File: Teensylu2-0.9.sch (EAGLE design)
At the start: 113 parts, among them J1 12VPWR, J10 HOTEND-2, J11 E1-THRM, J12 B-THRM, J13 E2-THRM, J2 MICROSD, J3 USB-MICRO-PTH, J4 FAN, J5 4P-TERM-BLOCK284391-4, J6 39-29-3066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

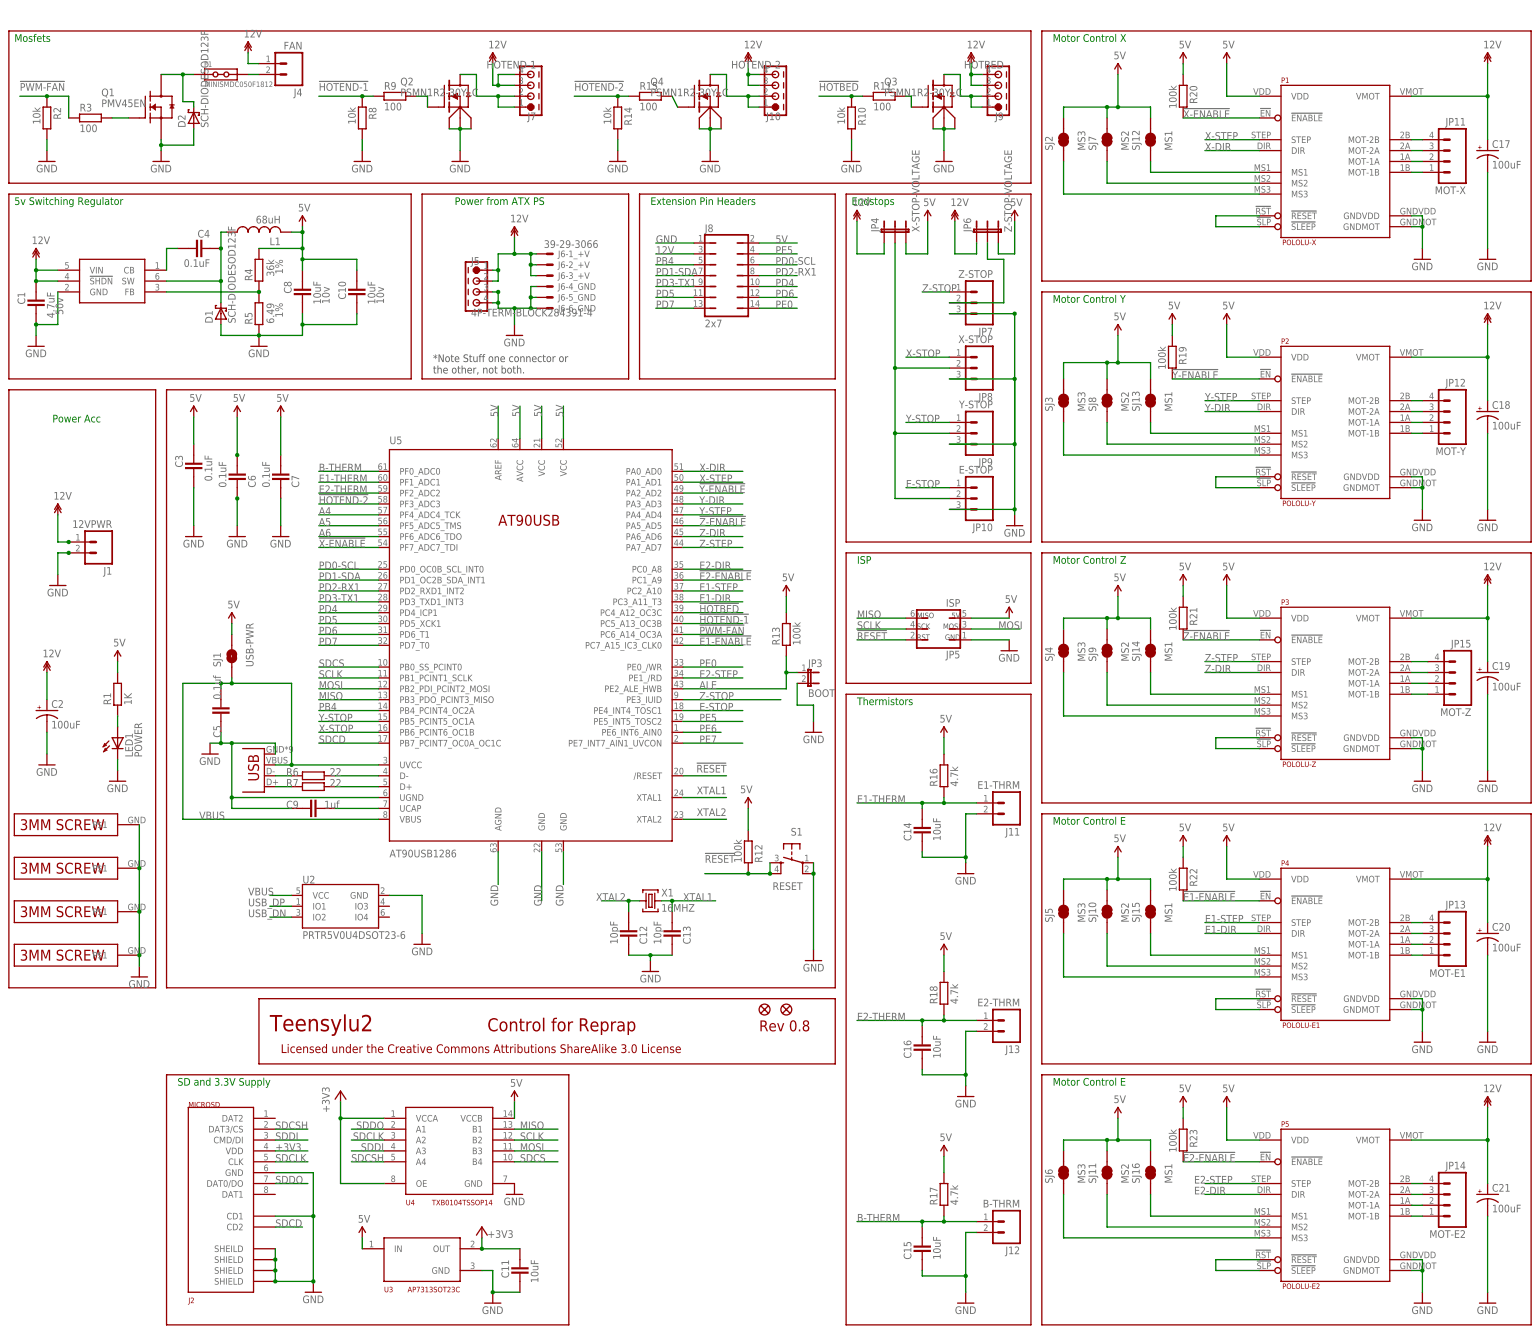
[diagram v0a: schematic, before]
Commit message: Production release
Pin mapping is added. Had to move a lot of pins around due to limitation
of the Teensyduino library.
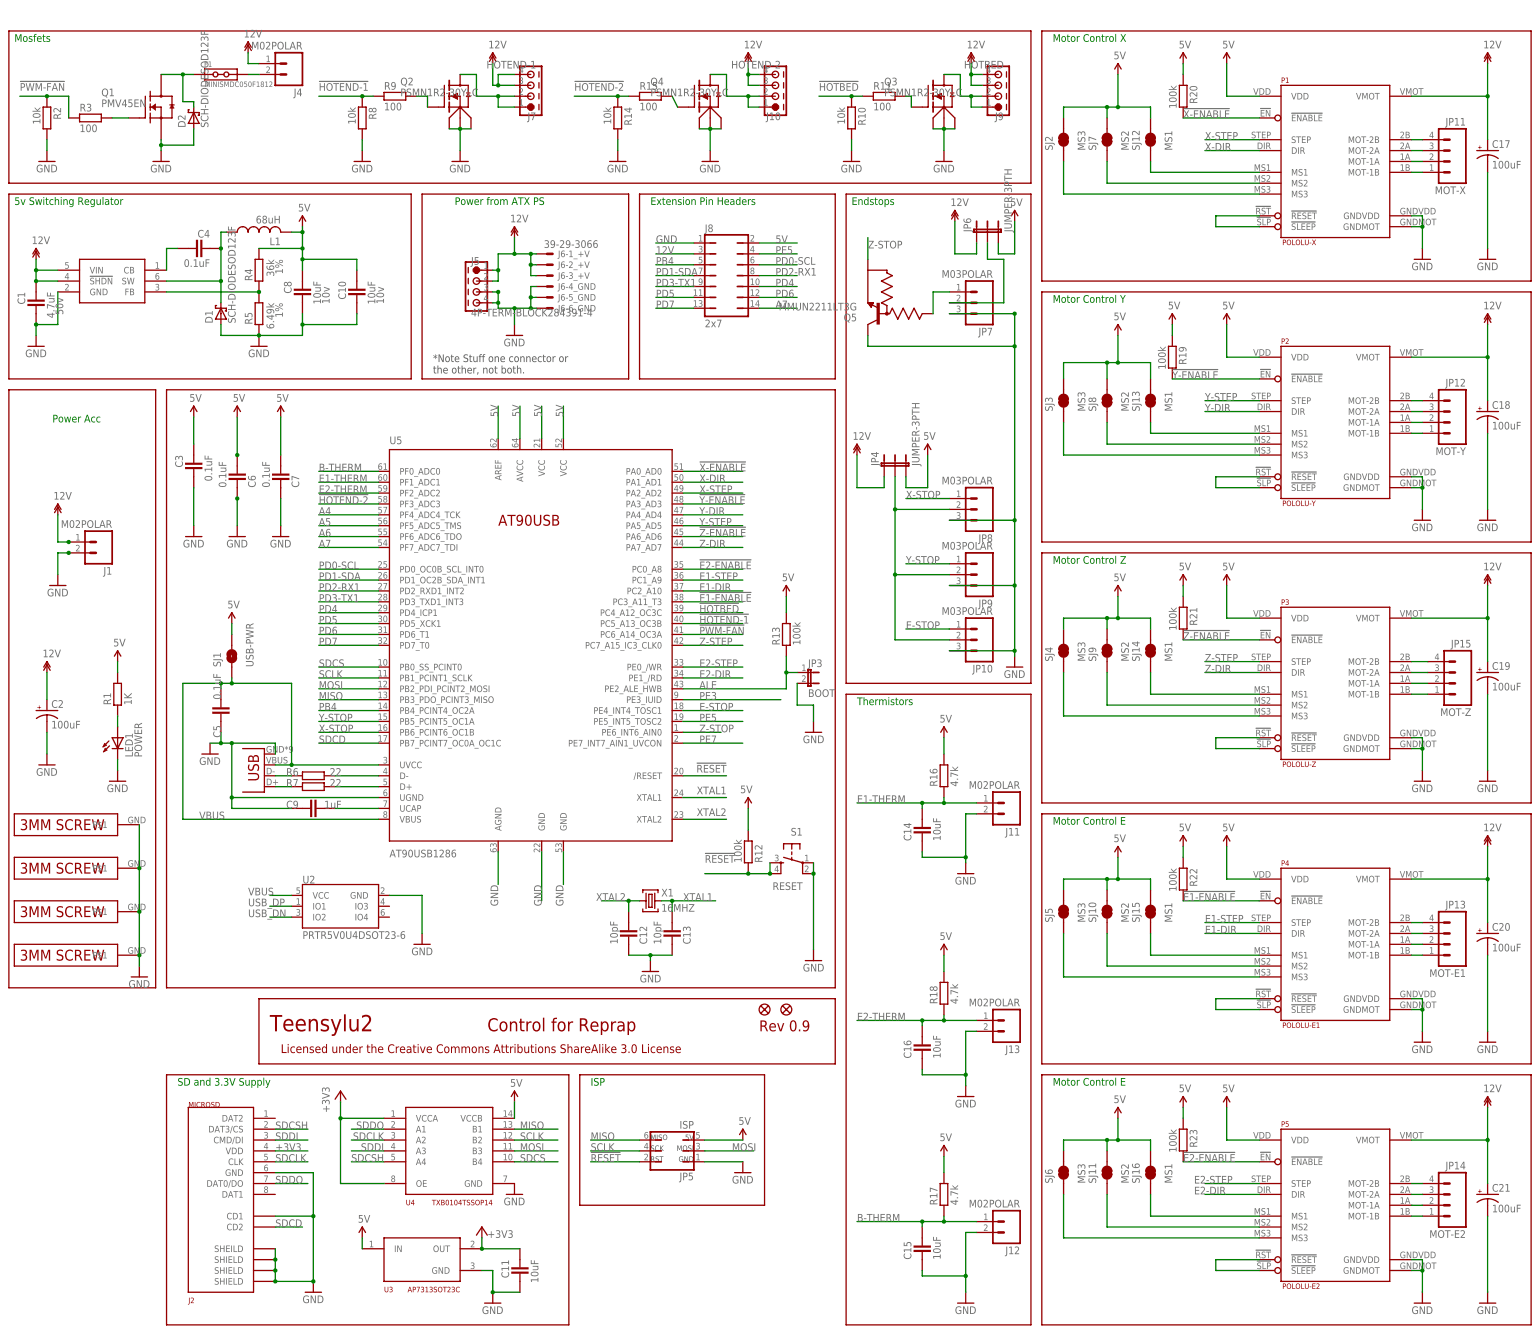
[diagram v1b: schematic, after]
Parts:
- added Q5: MMUN2211LT3G, teensylu:TRANSISTOR_NPN_BIASSOT23C
- C1: TOLERANCE (none) -> 10%
- C11, C14, C15, C16: VDC (none) -> 16V; VOLTAGE 16V -> (none)
- C12, C13: VDC (none) -> 50V; VOLTAGE 50V -> (none)
- C3, C7: VDC 16v -> 16V
- C5: value 0.1uf -> 0.1uF; MANUFACTURER (none) -> Murata; MANUFACTURER_PART_NUMBER (none) -> GRM188R71C104KA01D; TOLERANCE (none) -> 10%; VDC (none) -> 16V
- C9: value 1uf -> 1uF; VDC (none) -> 16V; VOLTAGE 16 -> (none)
- J1: value 12VPWR -> M02POLAR; DESCRIPTION (none) -> CONN HEADER 2POS .100 VERT TIN; MANUFACTURER (none) -> Molex; MANUFACTURER_PART_NUMBER (none) -> 0022272021; NOTES (none) -> Can use alternative part for Right Angle. MFG: TE Connectiv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
- J11: value E1-THRM -> M02POLAR; DESCRIPTION (none) -> CONN HEADER 2POS .100 VERT TIN; MANUFACTURER (none) -> Molex; MANUFACTURER_PART_NUMBER (none) -> 0022272021; NOTES (none) -> Can use alternative part for Right Angle. MFG: TE Connectiv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
- J12: value B-THRM -> M02POLAR; DESCRIPTION (none) -> CONN HEADER 2POS .100 VERT TIN; MANUFACTURER (none) -> Molex; MANUFACTURER_PART_NUMBER (none) -> 0022272021; NOTES (none) -> Can use alternative part for Right Angle. MFG: TE Connectiv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
- J13: value E2-THRM -> M02POLAR; DESCRIPTION (none) -> CONN HEADER 2POS .100 VERT TIN; MANUFACTURER (none) -> Molex; MANUFACTURER_PART_NUMBER (none) -> 0022272021; NOTES (none) -> Can use alternative part for Right Angle. MFG: TE Connectiv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
- J2: DESCRIPTION (none) -> CONN MICRO SD CARD PUSH-PULL R/A
- J4: value FAN -> M02POLAR; DESCRIPTION (none) -> CONN HEADER 2POS .100 VERT TIN; MANUFACTURER (none) -> Molex; MANUFACTURER_PART_NUMBER (none) -> 0022272021; NOTES (none) -> Can use alternative part for Right Angle. MFG: TE Connectiv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
- J8: DESCRIPTION (none) -> DIL VERTICAL PC TAIL PIN HEADER; MANUFACTURER (none) -> Harwin; MANUFACTURER_PART_NUMBER (none) -> M20-9980746
- JP10: value E-STOP -> M03POLAR; DESCRIPTION (none) -> CONN HEADER 3POS .100 VERT TIN; MANUFACTURER (none) -> Molex; MANUFACTURER_PART_NUMBER (none) -> 0022272031; NOTES (none) -> Can use alternative part for Right Angle. MFG: TE Connectiv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
- JP11, JP12, JP13, JP14, JP15: NOTES (none) -> Can use alternative part for Right Angle. MFG: TE Connectiv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
- JP3: DESCRIPTION (none) -> SIL VERTICAL PC TAIL PIN HEADER; MANUFACTURER (none) -> Harwin; MANUFACTURER_PART_NUMBER (none) -> M20-9990246
- JP4: value X-STOP-VOLTAGE -> JUMPER-3PTH
- JP6: value Z-STOP-VOLTAGE -> JUMPER-3PTH
- JP7: value Z-STOP -> M03POLAR; DESCRIPTION (none) -> CONN HEADER 3POS .100 VERT TIN; MANUFACTURER (none) -> Molex; MANUFACTURER_PART_NUMBER (none) -> 0022272031; NOTES (none) -> Can use alternative part for Right Angle. MFG: TE Connectiv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
- JP8: value X-STOP -> M03POLAR; DESCRIPTION (none) -> CONN HEADER 3POS .100 VERT TIN; MANUFACTURER (none) -> Molex; MANUFACTURER_PART_NUMBER (none) -> 0022272031; NOTES (none) -> Can use alternative part for Right Angle. MFG: TE Connectiv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
- JP9: value Y-STOP -> M03POLAR; DESCRIPTION (none) -> CONN HEADER 3POS .100 VERT TIN; MANUFACTURER (none) -> Molex; MANUFACTURER_PART_NUMBER (none) -> 0022272031; NOTES (none) -> Can use alternative part for Right Angle. MFG: TE Connectiv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
- R5: value 6.49 -> 6.49k
- U3: DESCRIPTION (none) -> IC REG LDO 3.3V 0.15A SOT23-3
- U4: DESCRIPTION (none) -> IC VOLT-LEVEL TRANSLATOR 14TSSOP
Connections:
- removed net PE0: J8.14, U5.PE0_/WR
- removed net PE6: U5.PE6_INT6_AIN0
- new net A7: J8.14, U5.PF7_ADC7_TDI
- new net PE3: U5.PE3_IUID
- new net Z-STOP-BIAS: JP7.1, Q5.B
- net !E1-ENABLE: now also U5.PC3_A11_T3; no longer U5.PC7_A15_IC3_CLK0
- net !E2-ENABLE: now also U5.PC0_A8; no longer U5.PC1_A9
- net !X-ENABLE: now also U5.PA0_AD0; no longer U5.PF7_ADC7_TDI
- net !Y-ENABLE: now also U5.PA3_AD3; no longer U5.PA2_AD2
- net !Z-ENABLE: now also U5.PA6_AD6; no longer U5.PA5_AD5
- net E1-DIR: now also U5.PC2_A10; no longer U5.PC3_A11_T3
- net E1-STEP: now also U5.PC1_A9; no longer U5.PC2_A10
- net E2-DIR: now also U5.PE1_/RD; no longer U5.PC0_A8
- net E2-STEP: now also U5.PE0_/WR; no longer U5.PE1_/RD
- net GND: now also Q5.C
- net X-DIR: now also U5.PA1_AD1; no longer U5.PA0_AD0
- net X-STEP: now also U5.PA2_AD2; no longer U5.PA1_AD1
- net Y-DIR: now also U5.PA4_AD4; no longer U5.PA3_AD3
- net Y-STEP: now also U5.PA5_AD5; no longer U5.PA4_AD4
- net Z-DIR: now also U5.PA7_AD7; no longer U5.PA6_AD6
- net Z-STEP: now also U5.PC7_A15_IC3_CLK0; no longer U5.PA7_AD7
- net Z-STOP: now also Q5.E, U5.PE6_INT6_AIN0; no longer JP7.1, U5.PE3_IUID
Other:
- note added: "Rev 0.9"
- note removed: "Rev 0.8"
- moved on the sheet: JP10, JP4, JP5, JP8, JP9
